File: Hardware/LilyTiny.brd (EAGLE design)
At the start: 20 x 20 mm, 14 parts, among them U1 ATTINY85

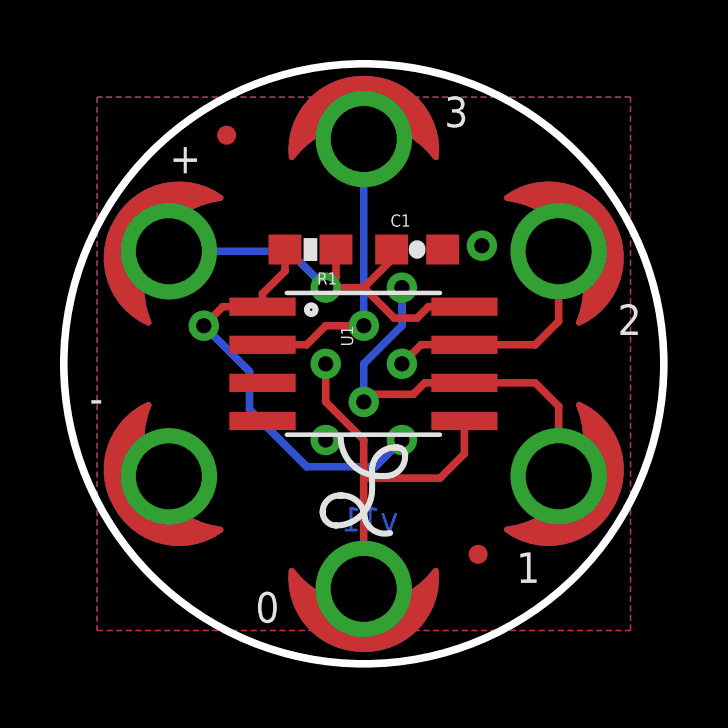
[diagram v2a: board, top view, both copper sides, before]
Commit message: Updating files to more clearly differentiate between Tiny/Twinkle
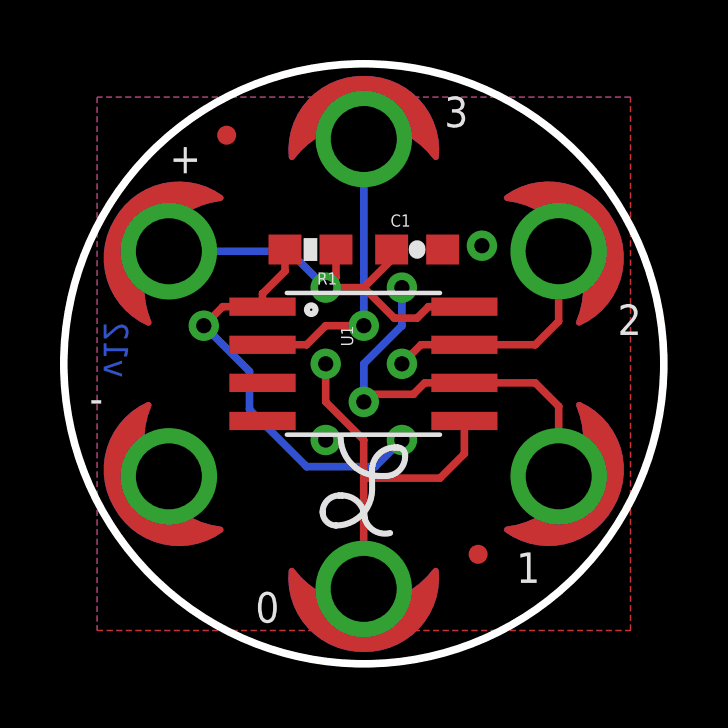
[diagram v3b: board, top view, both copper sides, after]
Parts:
- added LOGO2: SFE_LOGO_FLAME.1_INCH, SparkFun-Aesthetics:SFE_LOGO_FLAME_.1
- added U$1: REVISION, SparkFun-Aesthetics:REVISION
- moved FRAME2 39.0 mm to (-26.7, -20.3)
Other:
- board text added: "P. Lewis, T. Klopfenstein"
- board text added: "v12"
- board text removed: "Revised by Pete Lewis"
- board text removed: "v11"
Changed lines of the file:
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@@
 <?xml version="1.0" encoding="utf-8"?>
 <!DOCTYPE eagle SYSTEM "eagle.dtd">
-<eagle version="6.4">
+<eagle version="6.5.0">
 <drawing>
 <settings>
@@
 <setting verticaltext="up"/>
 </settings>
-<grid distance="0.05" unitdist="inch" unit="inch" style="lines" multiple="1" display="yes" altdistance="0.005" altunitdist="inch" altunit="inch"/>
+<grid distance="1" unitdist="mm" unit="mm" style="lines" multiple="1" display="yes" altdistance="0.1" altunitdist="mm" altunit="mm"/>
 <layers>
 <layer number="1" name="Top" color="4" fill="1" visible="yes" active="yes"/>
@@
 <text x="8.4602" y="0.962" size="1.016" layer="21" font="vector" ratio="15">2</text>
 <text x="-9.144" y="-1.651" size="1.016" layer="21" font="vector" ratio="15">-</text>
-<text x="40.64" y="-33.02" size="1.27" layer="27" font="vector" ratio="15">M. HORD</text>
+<text x="3.81" y="-20.32" size="1.27" layer="51" font="vector" ratio="15">M. HORD</text>
 <polygon width="0.2032" layer="29">
 <vertex x="-6" y="0"/>
@@
 <rectangle x1="2.54" y1="-2.286" x2="3.429" y2="-1.397" layer="22"/>
 <rectangle x1="4.064" y1="-2.286" x2="4.953" y2="-1.397" layer="22"/>
-<text x="1.143" y="-5.588" size="0.8128" layer="16" font="vector" ratio="25" rot="MR0">v11</text>
-<text x="49.53" y="-33.02" size="1.27" layer="27" font="vector" ratio="15">Revised by Pete Lewis</text>
+<text x="-7.857" y="1.412" size="0.8128" layer="16" font="vector" ratio="25" rot="MR270">v12</text>
+<text x="3.81" y="-22.86" size="1.27" layer="51" font="vector" ratio="15">P. Lewis, T. Klopfenstein</text>
 </plain>
 <attributes>
@@
 <element name="JP1" library="SparkFun" package="MICRO-FIDUCIAL" value="FIDUCIALUFIDUCIAL" x="-4.572" y="7.62"/>
 <element name="JP2" library="SparkFun" package="MICRO-FIDUCIAL" value="FIDUCIALUFIDUCIAL" x="3.81" y="-6.35"/>
-<element name="FRAME2" library="SparkFun-Aesthetics" package="CREATIVE_COMMONS" value="FRAME-LETTER" x="10.16" y="-33.02"/>
+<element name="FRAME2" library="SparkFun-Aesthetics" package="CREATIVE_COMMONS" value="FRAME-LETTER" x="-26.67" y="-20.32"/>
 <element name="LOGO1" library="SparkFun-Aesthetics" package="OSHW-LOGO-S" value="OSHW-LOGOS" x="-3.81" y="0" rot="MR90"/>
+<element name="U$1" library="SparkFun-Aesthetics" package="REVISION" value="REVISION" x="-15.24" y="-22.86"/>
+<element name="LOGO2" library="SparkFun-Aesthetics" package="SFE_LOGO_FLAME_.1" value="SFE_LOGO_FLAME.1_INCH" x="-2" y="-1" rot="MR90"/>
 </elements>
 <signals>

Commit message: Fixing silk errors from protos
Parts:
- moved LOGO1 4.49 mm to (-3.17, -4.45)
- moved LOGO2 4.07 mm to (-4.54, 2.17)
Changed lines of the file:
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@@
 <setting verticaltext="up"/>
 </settings>
-<grid distance="1" unitdist="mm" unit="mm" style="lines" multiple="1" display="yes" altdistance="0.1" altunitdist="mm" altunit="mm"/>
+<grid distance="0.0125" unitdist="inch" unit="inch" style="lines" multiple="1" display="yes" altdistance="0.005" altunitdist="inch" altunit="inch"/>
 <layers>
 <layer number="1" name="Top" color="4" fill="1" visible="yes" active="yes"/>
@@
 <layer number="47" name="Measures" color="7" fill="1" visible="no" active="yes"/>
 <layer number="48" name="Document" color="7" fill="1" visible="no" active="yes"/>
-<layer number="49" name="Reference" color="7" fill="1" visible="yes" active="yes"/>
+<layer number="49" name="Reference" color="7" fill="1" visible="no" active="yes"/>
 <layer number="50" name="dxf" color="7" fill="1" visible="no" active="yes"/>
 <layer number="51" name="tDocu" color="6" fill="1" visible="yes" active="yes"/>
@@
 <rectangle x1="2.54" y1="-2.286" x2="3.429" y2="-1.397" layer="22"/>
 <rectangle x1="4.064" y1="-2.286" x2="4.953" y2="-1.397" layer="22"/>
-<text x="-7.857" y="1.412" size="0.8128" layer="16" font="vector" ratio="25" rot="MR270">v12</text>
+<text x="-7.857" y="1.412" size="1.016" layer="16" font="vector" ratio="25" rot="MR270">v12</text>
 <text x="3.81" y="-22.86" size="1.27" layer="51" font="vector" ratio="15">P. Lewis, T. Klopfenstein</text>
+<wire x1="2.54" y1="2.54" x2="2.54" y2="1.27" width="0.254" layer="22"/>
+<wire x1="1.905" y1="2.8575" x2="1.905" y2="2.2225" width="0.2032" layer="22"/>
 </plain>
 <attributes>
@@
 <element name="JP2" library="SparkFun" package="MICRO-FIDUCIAL" value="FIDUCIALUFIDUCIAL" x="3.81" y="-6.35"/>
 <element name="FRAME2" library="SparkFun-Aesthetics" package="CREATIVE_COMMONS" value="FRAME-LETTER" x="-26.67" y="-20.32"/>
-<element name="LOGO1" library="SparkFun-Aesthetics" package="OSHW-LOGO-S" value="OSHW-LOGOS" x="-3.81" y="0" rot="MR90"/>
+<element name="LOGO1" library="SparkFun-Aesthetics" package="OSHW-LOGO-S" value="OSHW-LOGOS" x="-3.175" y="-4.445" rot="MR90"/>
 <element name="U$1" library="SparkFun-Aesthetics" package="REVISION" value="REVISION" x="-15.24" y="-22.86"/>
-<element name="LOGO2" library="SparkFun-Aesthetics" package="SFE_LOGO_FLAME_.1" value="SFE_LOGO_FLAME.1_INCH" x="-2" y="-1" rot="MR90"/>
+<element name="LOGO2" library="SparkFun-Aesthetics" package="SFE_LOGO_FLAME_.1" value="SFE_LOGO_FLAME.1_INCH" x="-4.54" y="2.175" rot="MR90"/>
 </elements>
 <signals>
